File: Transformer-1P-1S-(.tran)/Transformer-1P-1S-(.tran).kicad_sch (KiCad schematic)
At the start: 7 parts

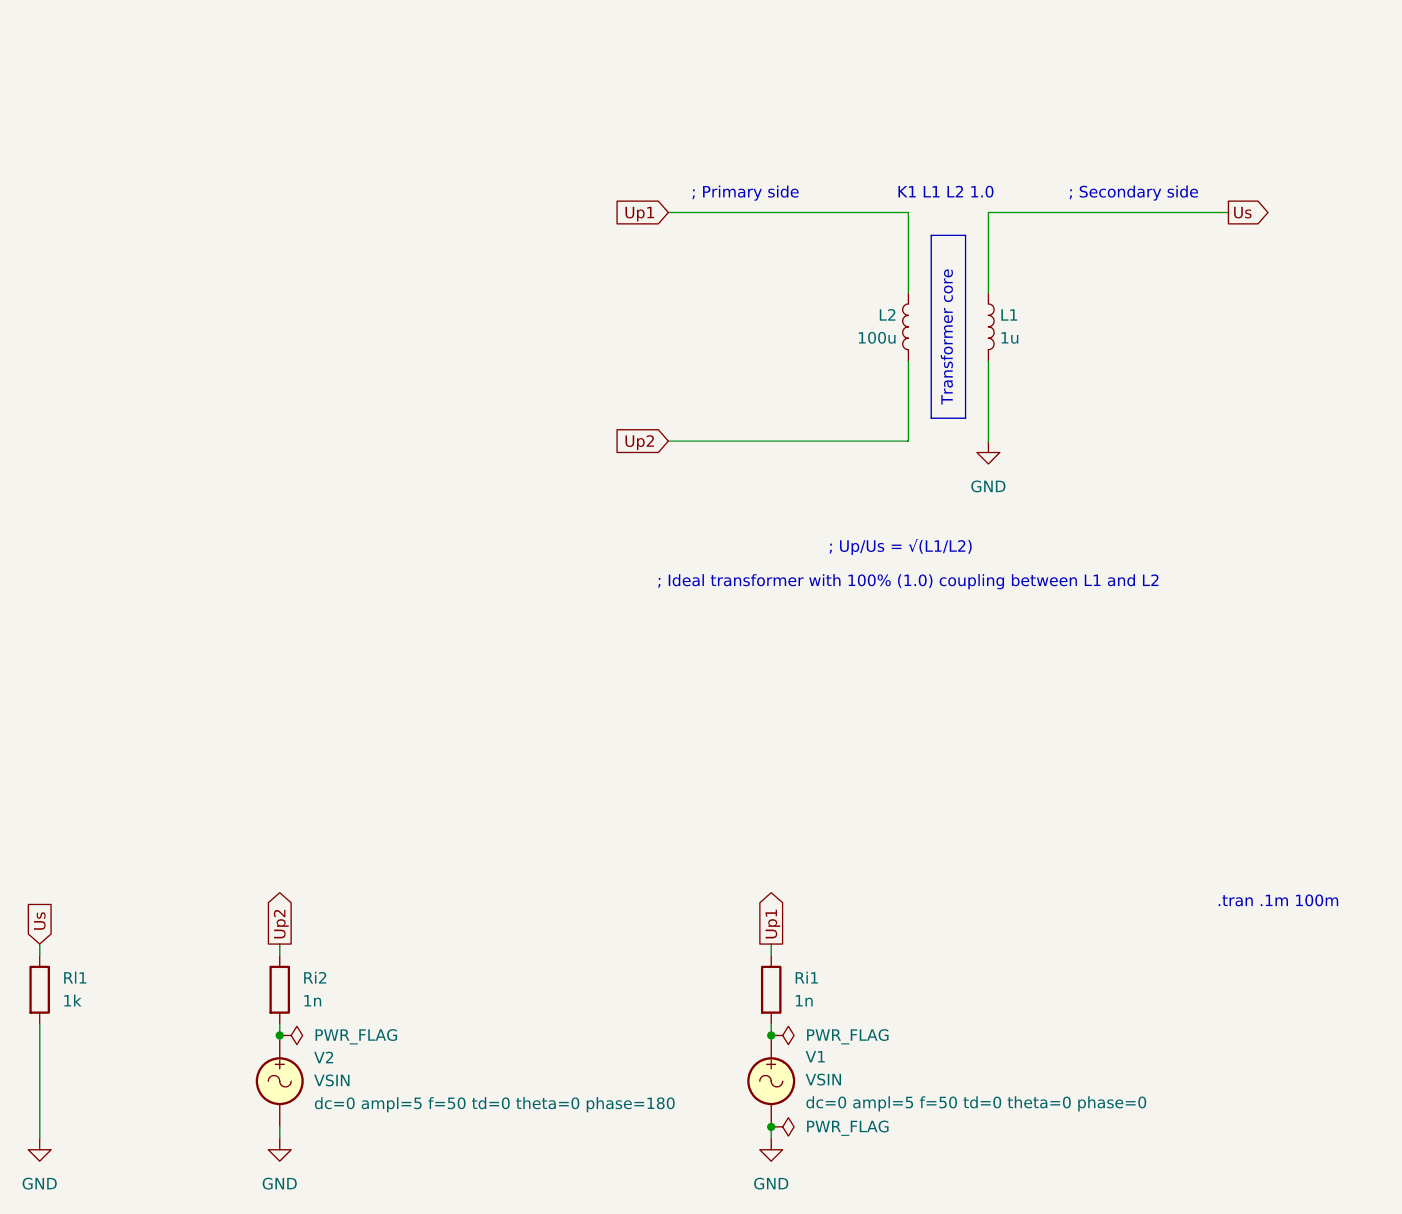
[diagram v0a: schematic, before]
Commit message: Updated all schematics and prepared for KiCad 8.0
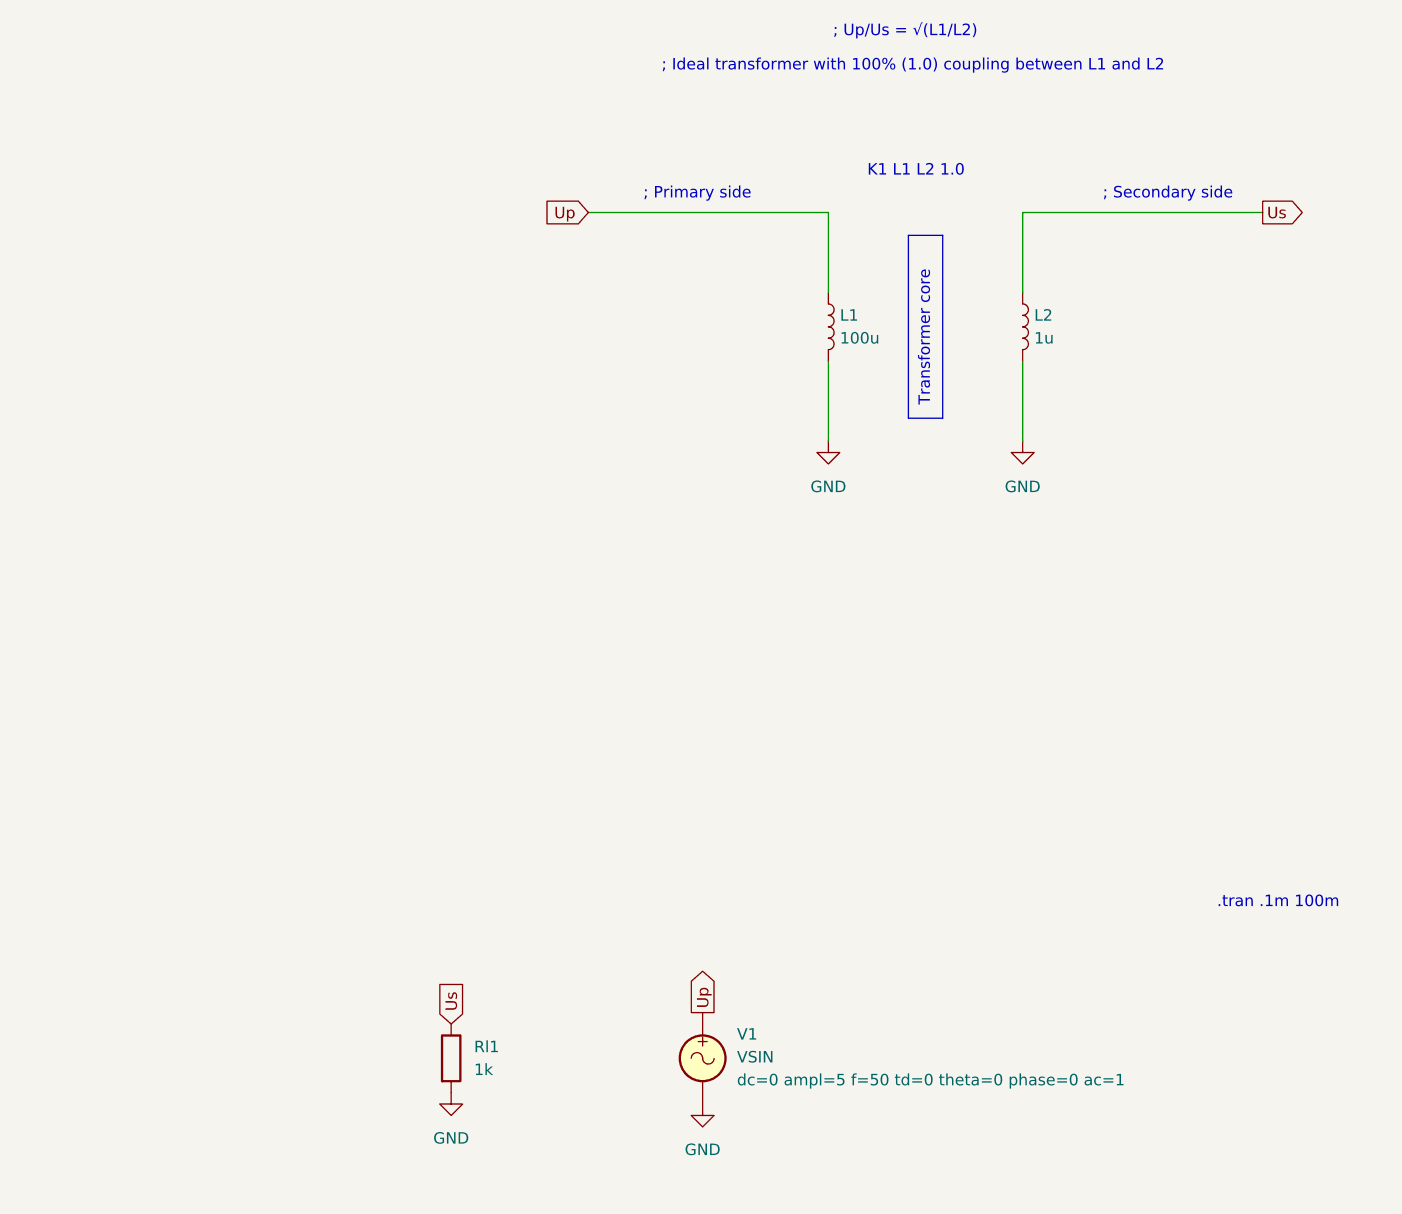
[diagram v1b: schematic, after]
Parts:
- removed Ri1, Ri2: 1n, symbol Device:R
- removed V2: VSIN, symbol Simulation_SPICE:VSIN
- L1: value 1u -> 100u
- L2: value 100u -> 1u
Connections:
- net Up1 is gone; now on net Us: L2.1
- net Up2 is gone; now on net GND: L2.2
- net Us: no longer L1.1
- net Up: now reaches V1.1
- net Up: now also L1.1
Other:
- moved on the sheet: Rl1
